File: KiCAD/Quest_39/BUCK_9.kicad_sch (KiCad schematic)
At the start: 32 parts, among them U40 AD626ANZ, U41 INA226, U42 LTM4611EV-PBF, U43 MCP4151-502E/SN

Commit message: Fixed INA226 schem. mistake and further layout work
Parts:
- added C153: 100nF, Capacitor_SMD:C_0603_1608Metric, symbol Device:C
- renumbered C140 to C149, C141 to C150, C142 to C151, C143 to C152, C144 to C154, C145 to C155, C146 to C156, C147 to C157, C148 to C158, C149 to C159, C150 to C160, C151 to C161, C152 to C162, C153 to C163
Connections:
- net +5V: now also C153.1
- net GND: now also C153.2
- net PV_POS: no longer C149.1, C150.1, C151.1, C152.1, R80.2, R82.1, R85.1, U42.A1 (VIN), U42.A2 (VIN), U42.A3 (VIN), U42.A4 (VIN), U42.A5 (VIN), U42.A6 (VIN), U42.B1 (VIN), U42.B2 (VIN), U42.B3 (VIN), U42.B4 (VIN), U42.B5 (VIN), U42.B6 (VIN), U42.C1 (VIN), U42.C2 (VIN), U42.C3 (VIN), U42.C4 (VIN), U42.C5 (VIN), U42.C6 (VIN)
- net Vin-: no longer TP70.1, U40.5 (OUT), U41.8 (Vbus)
- new net: TP70.1, U40.5 (OUT), U41.8 (Vbus)
- new net BUCK_VIN: C149.1, C150.1, C151.1, C152.1, R80.2, R82.1, R85.1, U42.A1 (VIN), U42.A2 (VIN), U42.A3 (VIN), U42.A4 (VIN), U42.A5 (VIN), U42.A6 (VIN), U42.B1 (VIN), U42.B2 (VIN), U42.B3 (VIN), U42.B4 (VIN), U42.B5 (VIN), U42.B6 (VIN), U42.C1 (VIN), U42.C2 (VIN), U42.C3 (VIN), U42.C4 (VIN), U42.C5 (VIN), U42.C6 (VIN)

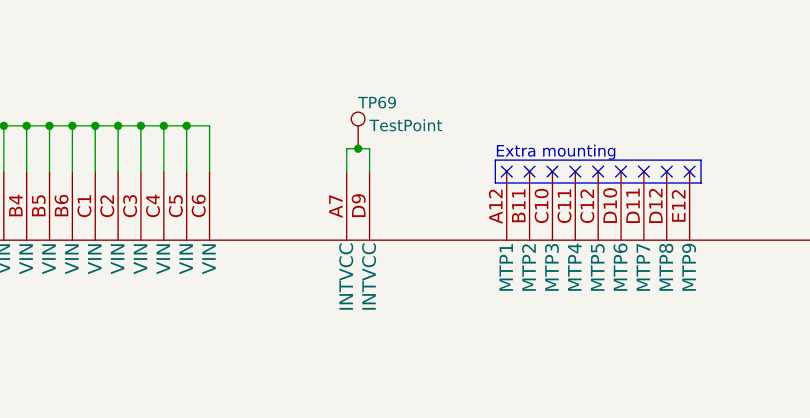
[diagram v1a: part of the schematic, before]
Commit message: Partial wiring of first buck converter section PCB layout
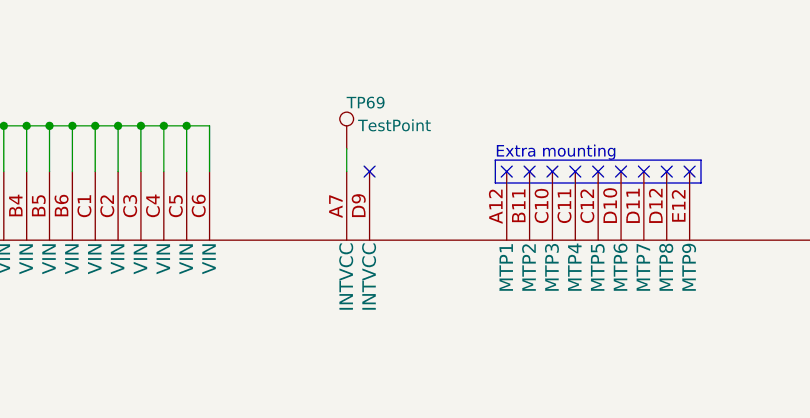
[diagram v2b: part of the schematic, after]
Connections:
- net at TP69.1, U42.A7 (INTVCC): no longer U42.D9 (INTVCC)
- no-connect marks 12 -> 13

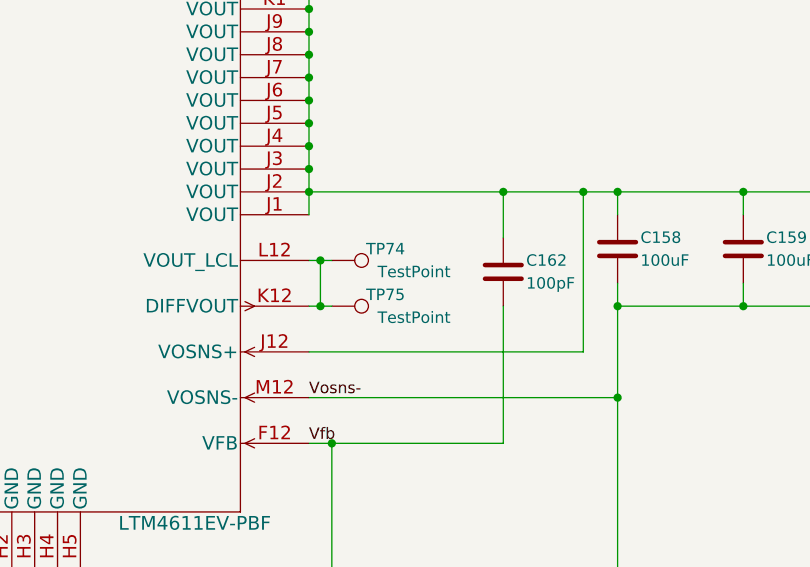
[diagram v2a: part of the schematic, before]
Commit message: Added 3rd buck converter section
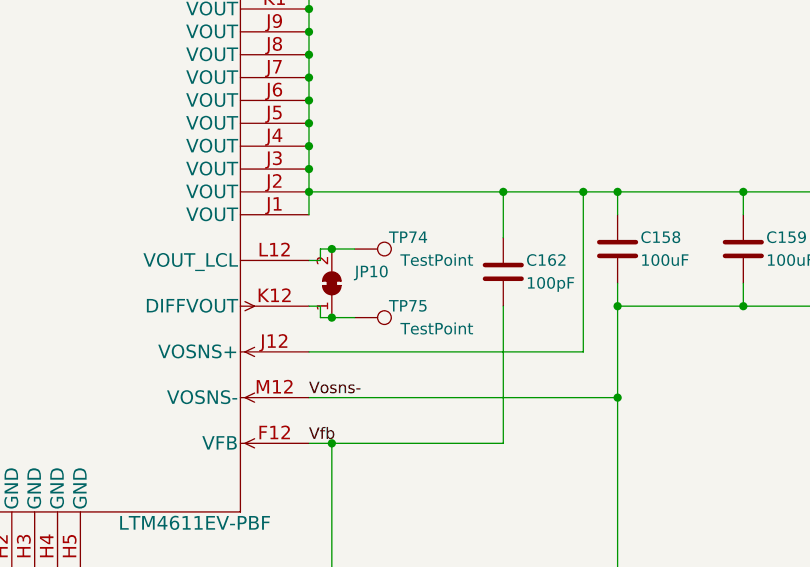
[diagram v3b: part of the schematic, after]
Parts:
- added JP10: SolderJumper_2_Bridged, Jumper:SolderJumper-2_P1.3mm_Bridged_RoundedPad1.0x1.5mm, symbol Jumper:SolderJumper_2_Bridged
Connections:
- net at TP75.1, U42.K12 (DIFFVOUT): now also JP10.1 (A); no longer TP74.1, U42.L12 (VOUT_LCL)
- new net: JP10.2 (B), TP74.1, U42.L12 (VOUT_LCL)
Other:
- moved on the sheet: TP74, TP75
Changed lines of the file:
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@@
   (junction (at 322.58 123.19) (diameter 0) (color 0 0 0 0)
   )
+  (junction (at 325.12 170.18) (diameter 0) (color 0 0 0 0)
+  )
   (junction (at 82.55 34.29) (diameter 0) (color 0 0 0 0)
   )
@@
   (junction (at 105.41 78.74) (diameter 0) (color 0 0 0 0)
   )
-  (junction (at 323.85 168.91) (diameter 0) (color 0 0 0 0)
-  )
   (junction (at 322.58 143.51) (diameter 0) (color 0 0 0 0)
   )
@@
   (junction (at 322.58 85.09) (diameter 0) (color 0 0 0 0)
   )
+  (junction (at 325.12 162.56) (diameter 0) (color 0 0 0 0)
+  )
   (junction (at 195.58 34.29) (diameter 0) (color 0 0 0 0)
   )
   (junction (at 175.26 34.29) (diameter 0) (color 0 0 0 0)
-  )
-  (junction (at 323.85 163.83) (diameter 0) (color 0 0 0 0)
   )
   (junction (at 167.64 199.39) (diameter 0) (color 0 0 0 0)
@@
     (stroke (width 0) (type default) (color 0 0 0 0))
   )
+  (wire (pts (xy 323.85 163.83) (xy 323.85 162.56))
+    (stroke (width 0) (type default) (color 0 0 0 0))
+  )
   (wire (pts (xy 213.36 34.29) (xy 215.9 34.29))
     (stroke (width 0) (type default) (color 0 0 0 0))
@@
     (stroke (width 0) (type default) (color 0 0 0 0))
   )
+  (wire (pts (xy 325.12 162.56) (xy 327.66 162.56))
+    (stroke (width 0) (type default) (color 0 0 0 0))
+  )
   (wire (pts (xy 322.58 82.55) (xy 322.58 85.09))
     (stroke (width 0) (type default) (color 0 0 0 0))
@@
     (stroke (width 0) (type default) (color 0 0 0 0))
   )
-  (wire (pts (xy 323.85 163.83) (xy 325.12 163.83))
-    (stroke (width 0) (type default) (color 0 0 0 0))
-  )
   (wire (pts (xy 129.54 59.69) (xy 139.7 59.69))
     (stroke (width 0) (type default) (color 0 0 0 0))
@@
     (stroke (width 0) (type default) (color 0 0 0 0))
   )
+  (wire (pts (xy 323.85 170.18) (xy 325.12 170.18))
+    (stroke (width 0) (type default) (color 0 0 0 0))
+  )
   (wire (pts (xy 25.4 81.28) (xy 25.4 82.55))
     (stroke (width 0) (type default) (color 0 0 0 0))
@@
     (stroke (width 0) (type default) (color 0 0 0 0))
   )
+  (wire (pts (xy 322.58 163.83) (xy 323.85 163.83))
+    (stroke (width 0) (type default) (color 0 0 0 0))
+  )
   (wire (pts (xy 325.12 212.09) (xy 325.12 220.98))
     (stroke (width 0) (type default) (color 0 0 0 0))
@@
     (stroke (width 0) (type default) (color 0 0 0 0))
   )
-  (wire (pts (xy 325.12 168.91) (xy 323.85 168.91))
-    (stroke (width 0) (type default) (color 0 0 0 0))
-  )
   (wire (pts (xy 210.82 34.29) (xy 210.82 39.37))
     (stroke (width 0) (type default) (color 0 0 0 0))
@@
     (stroke (width 0) (type default) (color 0 0 0 0))
   )
+  (wire (pts (xy 323.85 168.91) (xy 323.85 170.18))
+    (stroke (width 0) (type default) (color 0 0 0 0))
+  )
   (wire (pts (xy 322.58 74.93) (xy 322.58 72.39))
     (stroke (width 0) (type default) (color 0 0 0 0))
@@
     (stroke (width 0) (type default) (color 0 0 0 0))
   )
+  (wire (pts (xy 323.85 162.56) (xy 325.12 162.56))
+    (stroke (width 0) (type default) (color 0 0 0 0))
+  )
   (wire (pts (xy 322.58 128.27) (xy 322.58 130.81))
     (stroke (width 0) (type default) (color 0 0 0 0))
@@
     (stroke (width 0) (type default) (color 0 0 0 0))
   )
-  (wire (pts (xy 322.58 163.83) (xy 323.85 163.83))
-    (stroke (width 0) (type default) (color 0 0 0 0))
-  )
   (wire (pts (xy 200.66 199.39) (xy 203.2 199.39))
     (stroke (width 0) (type default) (color 0 0 0 0))
@@
     (stroke (width 0) (type default) (color 0 0 0 0))
   )
+  (wire (pts (xy 325.12 170.18) (xy 327.66 170.18))
+    (stroke (width 0) (type default) (color 0 0 0 0))
+  )
   (wire (pts (xy 322.58 74.93) (xy 322.58 77.47))
     (stroke (width 0) (type default) (color 0 0 0 0))
@@
     (stroke (width 0) (type default) (color 0 0 0 0))
   )
-  (wire (pts (xy 323.85 163.83) (xy 323.85 168.91))
-    (stroke (width 0) (type default) (color 0 0 0 0))
-  )
   (wire (pts (xy 198.12 34.29) (xy 198.12 39.37))
     (stroke (width 0) (type default) (color 0 0 0 0))
@@
     (stroke (width 0) (type default) (color 0 0 0 0))
   )
-  (wire (pts (xy 323.85 168.91) (xy 322.58 168.91))
-    (stroke (width 0) (type default) (color 0 0 0 0))
-  )
   (wire (pts (xy 193.04 34.29) (xy 193.04 39.37))
     (stroke (width 0) (type default) (color 0 0 0 0))
@@
   )
   (wire (pts (xy 82.55 60.96) (xy 82.55 83.82))
+    (stroke (width 0) (type default) (color 0 0 0 0))
+  )
+  (wire (pts (xy 322.58 168.91) (xy 323.85 168.91))
     (stroke (width 0) (type default) (color 0 0 0 0))
   )
@@
     )
     (pin "1")
+  )
+  (symbol (lib_id "Jumper:SolderJumper_2_Bridged") (at 325.12 166.37 90) (unit 1)
+    (in_bom yes) (on_board yes) (fields_autoplaced)
+    (property "Reference" "JP10" (id 0) (at 327.66 165.0999 90)
+      (effects (font (size 1.27 1.27)) (justify right))
+    )
+    (property "Value" "SolderJumper_2_Bridged" (id 1) (at 327.66 167.6399 90)
+      (effects (font (size 1.27 1.27)) (justify right) hide)
+    )
+    (property "Footprint" "Jumper:SolderJumper-2_P1.3mm_Bridged_RoundedPad1.0x1.5mm" (id 2) (at 325.12 166.37 0)
+      (effects (font (size 1.27 1.27)) hide)
+    )
+    (property "Datasheet" "~" (id 3) (at 325.12 166.37 0)
+      (effects (font (size 1.27 1.27)) hide)
+    )
+    (pin "1")
+    (pin "2")
   )
   (symbol (lib_id "LTM4611EV:LTM4611EV-PBF") (at 137.16 97.79 0) (unit 1)
@@
     (pin "2")
   )
-  (symbol (lib_id "Connector:TestPoint") (at 325.12 163.83 270) (unit 1)
-    (in_bom yes) (on_board yes)
-    (property "Reference" "TP74" (id 0) (at 328.93 162.56 90)
-      (effects (font (size 1.27 1.27)) (justify left))
-    )
-    (property "Value" "TestPoint" (id 1) (at 330.2 165.1 90)
-      (effects (font (size 1.27 1.27)) (justify left))
-    )
-    (property "Footprint" "TestPoint:TestPoint_Pad_D2.0mm" (id 2) (at 325.12 168.91 0)
-      (effects (font (size 1.27 1.27)) hide)
-    )
-    (property "Datasheet" "~" (id 3) (at 325.12 168.91 0)
+  (symbol (lib_id "Connector:TestPoint") (at 327.66 162.56 270) (unit 1)
+    (in_bom yes) (on_board yes)
+    (property "Reference" "TP74" (id 0) (at 331.47 161.29 90)
+      (effects (font (size 1.27 1.27)) (justify left))
+    )
+    (property "Value" "TestPoint" (id 1) (at 332.74 163.83 90)
+      (effects (font (size 1.27 1.27)) (justify left))
+    )
+    (property "Footprint" "TestPoint:TestPoint_Pad_D2.0mm" (id 2) (at 327.66 167.64 0)
+      (effects (font (size 1.27 1.27)) hide)
+    )
+    (property "Datasheet" "~" (id 3) (at 327.66 167.64 0)
       (effects (font (size 1.27 1.27)) hide)
     )
@@
     (pin "2")
   )
-  (symbol (lib_id "Connector:TestPoint") (at 325.12 168.91 270) (unit 1)
-    (in_bom yes) (on_board yes)
-    (property "Reference" "TP75" (id 0) (at 328.93 167.64 90)
-      (effects (font (size 1.27 1.27)) (justify left))
-    )
-    (property "Value" "TestPoint" (id 1) (at 330.2 170.18 90)
-      (effects (font (size 1.27 1.27)) (justify left))
-    )
-    (property "Footprint" "TestPoint:TestPoint_Pad_D2.0mm" (id 2) (at 325.12 173.99 0)
-      (effects (font (size 1.27 1.27)) hide)
-    )
-    (property "Datasheet" "~" (id 3) (at 325.12 173.99 0)
-      (effects (font (size 1.27 1.27)) hide)
-    )
+  (symbol (lib_id "Connector:TestPoint") (at 327.66 170.18 270) (unit 1)
+    (in_bom yes) (on_board yes)
+    (property "Reference" "TP75" (id 0) (at 331.47 168.91 90)
+      (effects (font (size 1.27 1.27)) (justify left))
+    )
+    (property "Value" "TestPoint" (id 1) (at 332.74 171.45 90)
+      (effects (font (size 1.27 1.27)) (justify left))
+    )
+    (property "Footprint" "TestPoint:TestPoint_Pad_D2.0mm" (id 2) (at 327.66 175.26 0)
+      (effects (font (size 1.27 1.27)) hide)
+    )
+    (property "Datasheet" "~" (id 3) (at 327.66 175.26 0)
+      (effects (font (size 1.27 1.27)) hide)
+    )

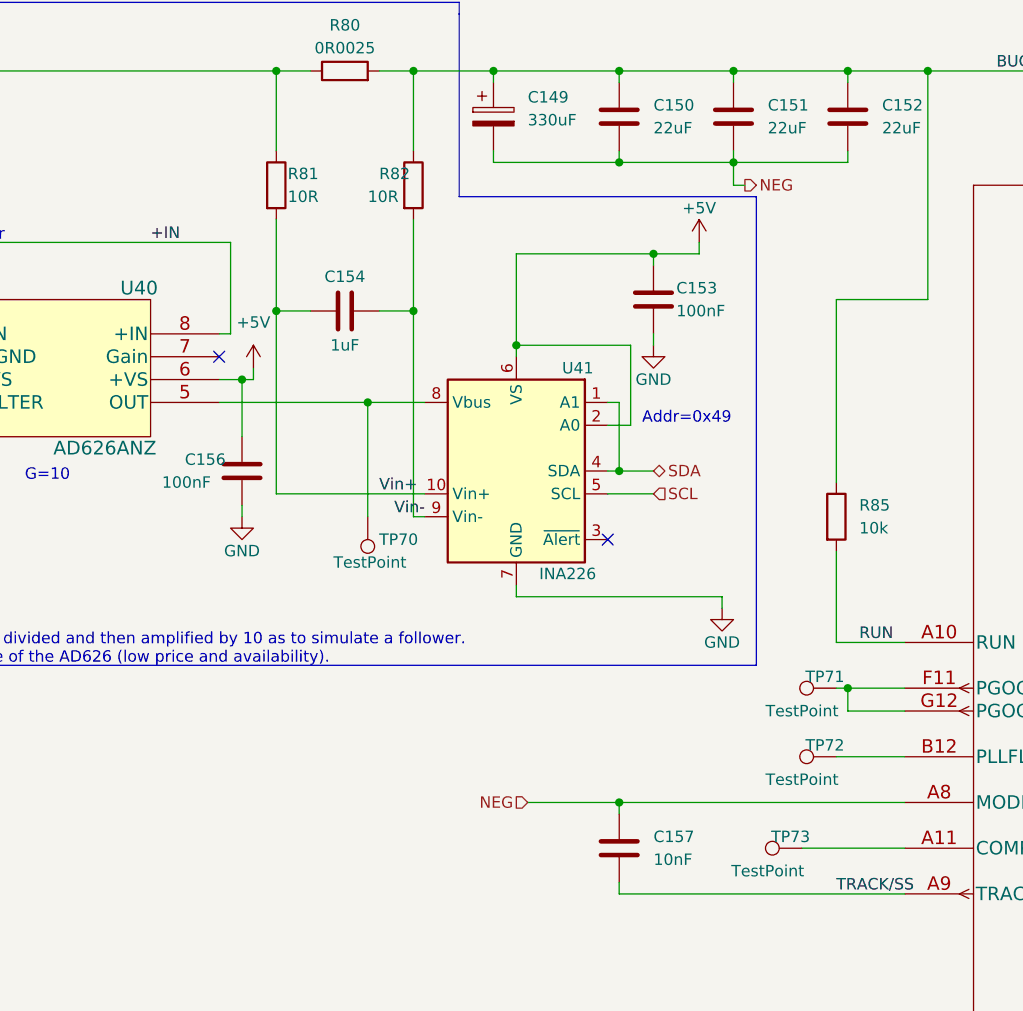
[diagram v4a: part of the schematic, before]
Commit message: Redid layout for the LTM4611EV Buck-converters (Issues with net-assignment to IC pads)
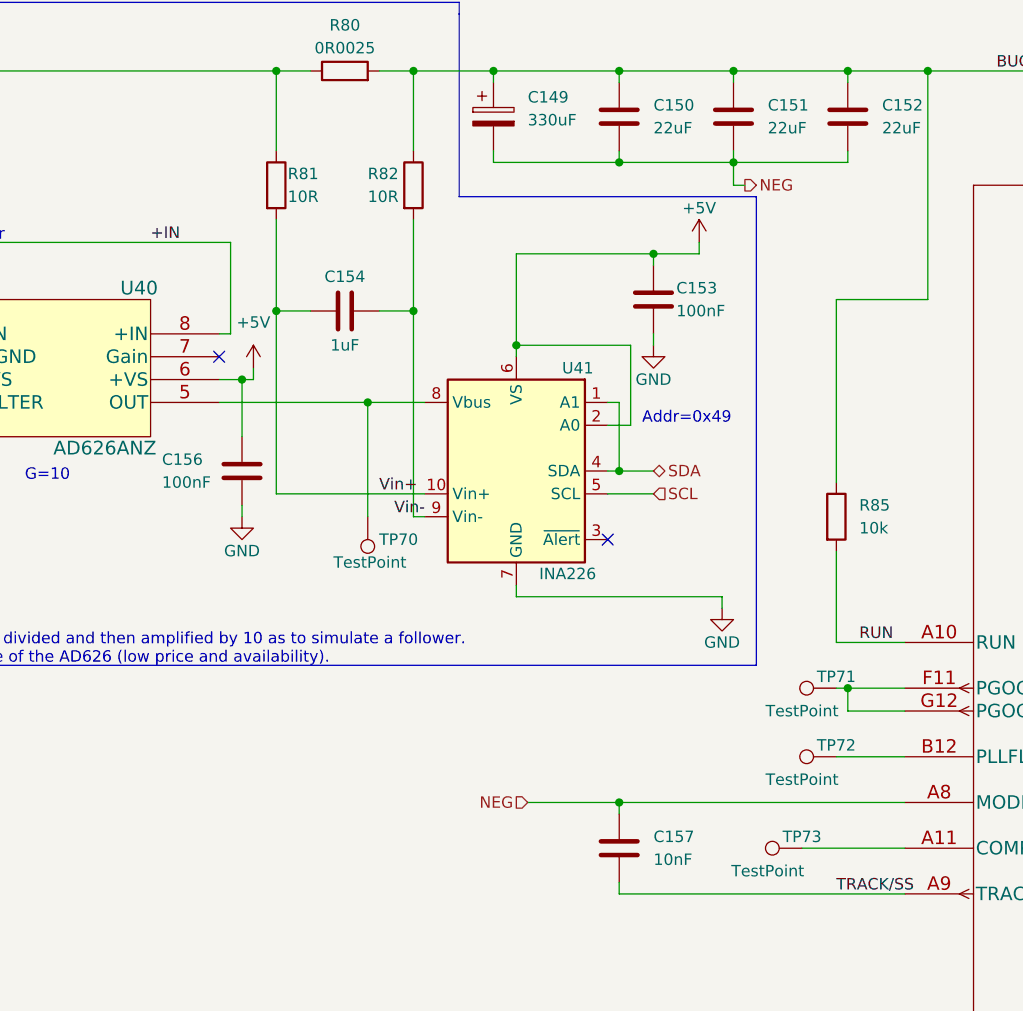
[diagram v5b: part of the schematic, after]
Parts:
- U40: footprint Package_DIP:DIP-8_W8.89mm_SMDSocket_LongPads -> Package_DIP:DIP-8_W7.62mm_Socket_LongPads
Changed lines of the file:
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@@
   (symbol (lib_id "Connector:TestPoint") (at 129.54 102.87 90) (unit 1)
     (in_bom yes) (on_board yes)
-    (property "Reference" "TP71" (id 0) (at 128.27 101.6 90))
+    (property "Reference" "TP71" (id 0) (at 129.54 101.6 90))
     (property "Value" "TestPoint" (id 1) (at 125.73 105.41 90))
     (property "Footprint" "TestPoint:TestPoint_Pad_D2.0mm" (id 2) (at 129.54 97.79 0)
@@
   (symbol (lib_id "Connector:TestPoint") (at 125.73 120.65 90) (unit 1)
     (in_bom yes) (on_board yes)
-    (property "Reference" "TP73" (id 0) (at 124.46 119.38 90))
+    (property "Reference" "TP73" (id 0) (at 125.73 119.38 90))
     (property "Value" "TestPoint" (id 1) (at 121.92 123.19 90))
     (property "Footprint" "TestPoint:TestPoint_Pad_D2.0mm" (id 2) (at 125.73 115.57 0)
@@
   (symbol (lib_id "Device:R") (at 82.55 46.99 0) (unit 1)
     (in_bom yes) (on_board yes)
-    (property "Reference" "R82" (id 0) (at 78.74 45.72 0)
+    (property "Reference" "R82" (id 0) (at 77.47 45.72 0)
       (effects (font (size 1.27 1.27)) (justify left))
     )
@@
       (effects (font (size 1.524 1.524)))
     )
-    (property "Footprint" "Package_DIP:DIP-8_W8.89mm_SMDSocket_LongPads" (id 2) (at 44.45 58.674 0)
+    (property "Footprint" "Package_DIP:DIP-8_W7.62mm_Socket_LongPads" (id 2) (at 44.45 58.674 0)
       (effects (font (size 1.524 1.524)) hide)
     )
@@
   (symbol (lib_id "Device:C") (at 63.5 78.74 0) (unit 1)
     (in_bom yes) (on_board yes)
-    (property "Reference" "C156" (id 0) (at 57.15 77.47 0)
+    (property "Reference" "C156" (id 0) (at 54.61 77.47 0)
       (effects (font (size 1.27 1.27)) (justify left))
     )
@@
   (symbol (lib_id "Connector:TestPoint") (at 129.54 110.49 90) (unit 1)
     (in_bom yes) (on_board yes)
-    (property "Reference" "TP72" (id 0) (at 128.27 109.22 90))
+    (property "Reference" "TP72" (id 0) (at 129.54 109.22 90))
     (property "Value" "TestPoint" (id 1) (at 125.73 113.03 90))
     (property "Footprint" "TestPoint:TestPoint_Pad_D2.0mm" (id 2) (at 129.54 105.41 0)

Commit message: Added all the SolidWorks files, edited README
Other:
- title: (none) -> BUCK_9
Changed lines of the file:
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@@
 (kicad_sch (version 20211123) (generator eeschema)
   (paper "A3")
+  (title_block
+    (title "BUCK_9")
+    (date "2023-01-31")
+    (rev "1.0")
+  )
   (junction (at 165.1 199.39) (diameter 0) (color 0 0 0 0)
   )
